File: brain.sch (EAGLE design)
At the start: 9 parts, among them IC1 MCP1253-33X50

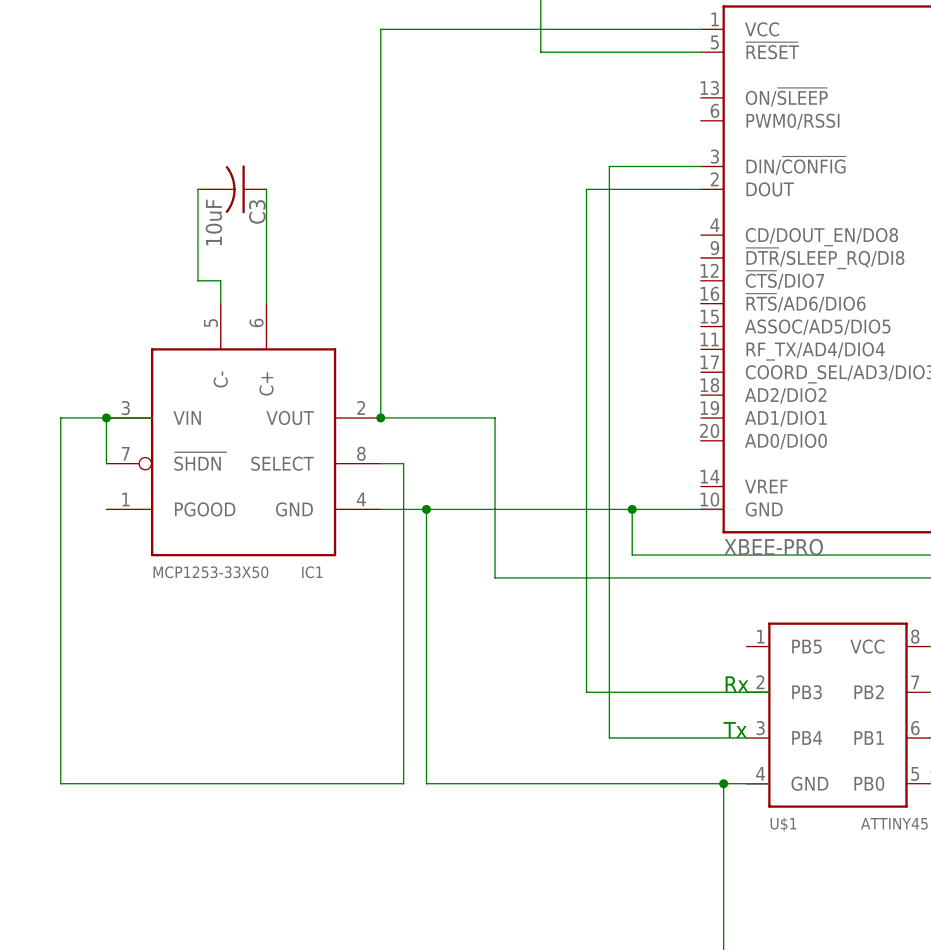
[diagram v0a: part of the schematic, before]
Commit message: Changed to using the TI LDO for the voltage regulation. Created and added symbol for the Sunny Buddy mounting to allow routing tools to see the electrical connections.
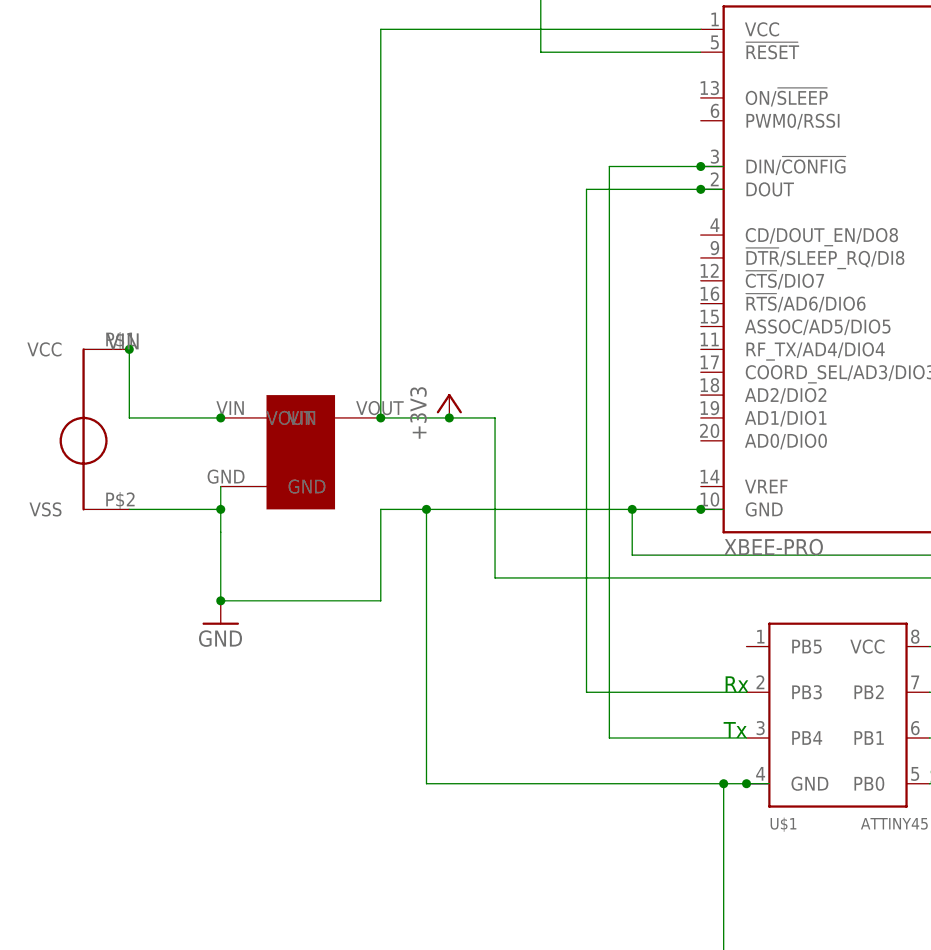
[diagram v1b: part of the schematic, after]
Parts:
- removed C3: 10uF, rcl:C-US050-045X075
- removed IC1: MCP1253-33X50, microchip-MCP125x-xxx:MCP1253-33X50
- added U$2: LP2950, seniordesign:LP2950
- added U$3: SUNNYBUDDYMOUNT, seniordesign:SUNNYBUDDYMOUNT
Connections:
- removed net BAT: IC1.SELECT, IC1.SHDN, IC1.VIN
- removed net N$1: IC1.VOUT, U$1.VCC, XB1.VCC
- removed net N$10: C3.1, IC1.C+
- removed net N$12: C3.2, IC1.C-
- removed net N$5: IC1.GND, R1.2, R2.2, S1.S1
- new net +3V3: U$1.VCC, U$2.VOUT, XB1.VCC
- new net GND: R1.2, R2.2, S1.S1, U$1.GND, U$2.GND, U$3.VSS, XB1.GND
- new net VIN: U$2.VIN, U$3.VCC
- net N$14: now also U$1.PB3
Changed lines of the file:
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@@
 <attribute name="OC_NEWARK" value="unknown"/>
-</part>
-<part name="IC1" library="microchip-MCP125x-xxx" deviceset="MCP1253-33X50" device="">
-<attribute name="MF" value=""/>
-<attribute name="MPN" value="LT3652EMSE#TRPBF"/>
-<attribute name="OC_NEWARK" value="64R8540"/>
 </part>
 <part name="U$1" library="attiny45" deviceset="ATTINY45" device="">
@@
 </part>
 <part name="S1" library="switch-omron" deviceset="10-XX" device=""/>
-<part name="C3" library="rcl" deviceset="C-US" device="050-045X075" value="10uF"/>
 <part name="U2" library="SparkFun-Connectors" deviceset="AUDIO-JACK" device="PTH"/>
 <part name="U3" library="SparkFun-Connectors" deviceset="AUDIO-JACK" device="PTH"/>
+<part name="GND1" library="supply1" deviceset="GND" device=""/>
+<part name="U$2" library="seniordesign" deviceset="LP2950" device=""/>
+<part name="+3V1" library="supply1" deviceset="+3V3" device=""/>
+<part name="U$3" library="seniordesign" deviceset="SUNNYBUDDYMOUNT" device=""/>
 </parts>
 <sheets>
@@
 <instances>
 <instance part="XB1" gate="G$1" x="76.2" y="43.18"/>
-<instance part="IC1" gate="G$1" x="10.16" y="22.86">
-<attribute name="OC_NEWARK" x="10.16" y="22.86" size="1.778" layer="96" display="off"/>
-<attribute name="MF" x="10.16" y="22.86" size="1.778" layer="96" display="off"/>
-<attribute name="MPN" x="10.16" y="22.86" size="1.778" layer="96" display="off"/>
-</instance>
 <instance part="U$1" gate="G$1" x="76.2" y="-7.62">
 <attribute name="OC_NEWARK" x="76.2" y="-7.62" size="1.778" layer="96" display="off"/>
@@
 </instance>
 <instance part="S1" gate="1" x="137.16" y="45.72" rot="R270"/>
-<instance part="C3" gate="G$1" x="10.16" y="50.8" rot="R270"/>
 <instance part="U2" gate="G$1" x="129.54" y="-10.16"/>
 <instance part="U3" gate="G$1" x="129.54" y="-33.02"/>
+<instance part="GND1" gate="1" x="7.62" y="2.54"/>
+<instance part="U$2" gate="G$1" x="17.78" y="20.32"/>
+<instance part="+3V1" gate="G$1" x="33.02" y="27.94"/>
+<instance part="U$3" gate="G$1" x="-7.62" y="25.4"/>
 </instances>
 <busses>
 </busses>
 <nets>
-<net name="N$1" class="0">
-<segment>
-<pinref part="IC1" gate="G$1" pin="VOUT"/>
-<pinref part="XB1" gate="G$1" pin="VCC"/>
-<wire x1="25.4" y1="25.4" x2="25.4" y2="68.58" width="0.1524" layer="91"/>
-<wire x1="25.4" y1="68.58" x2="60.96" y2="68.58" width="0.1524" layer="91"/>
-<pinref part="U$1" gate="G$1" pin="VCC"/>
-<wire x1="86.36" y1="0" x2="88.9" y2="0" width="0.1524" layer="91"/>
-<wire x1="88.9" y1="0" x2="88.9" y2="7.62" width="0.1524" layer="91"/>
-<wire x1="88.9" y1="7.62" x2="38.1" y2="7.62" width="0.1524" layer="91"/>
-<wire x1="38.1" y1="7.62" x2="38.1" y2="25.4" width="0.1524" layer="91"/>
-<wire x1="38.1" y1="25.4" x2="25.4" y2="25.4" width="0.1524" layer="91"/>
-<junction x="25.4" y="25.4"/>
-</segment>
-</net>
 <net name="N$3" class="0">
 <segment>
@@
 </segment>
 </net>
-<net name="N$5" class="0">
-<segment>
-<pinref part="IC1" gate="G$1" pin="GND"/>
+<net name="GND" class="0">
+<segment>
 <wire x1="25.4" y1="15.24" x2="30.48" y2="15.24" width="0.1524" layer="91"/>
-<wire x1="63.5" y1="15.24" x2="53.34" y2="15.24" width="0.1524" layer="91"/>
+<wire x1="63.5" y1="15.24" x2="60.96" y2="15.24" width="0.1524" layer="91"/>
+<wire x1="60.96" y1="15.24" x2="53.34" y2="15.24" width="0.1524" layer="91"/>
 <wire x1="53.34" y1="15.24" x2="30.48" y2="15.24" width="0.1524" layer="91"/>
 <wire x1="30.48" y1="15.24" x2="30.48" y2="-15.24" width="0.1524" layer="91"/>
@@
 <pinref part="R1" gate="G$1" pin="2"/>
 <pinref part="R2" gate="G$1" pin="2"/>
-<wire x1="63.5" y1="-15.24" x2="68.58" y2="-15.24" width="0.1524" layer="91"/>
+<wire x1="63.5" y1="-15.24" x2="66.04" y2="-15.24" width="0.1524" layer="91"/>
+<wire x1="66.04" y1="-15.24" x2="68.58" y2="-15.24" width="0.1524" layer="91"/>
 <wire x1="167.64" y1="-10.16" x2="167.64" y2="-35.56" width="0.1524" layer="91"/>
 <wire x1="167.64" y1="-35.56" x2="167.64" y2="-45.72" width="0.1524" layer="91"/>
@@
 <junction x="167.64" y="-35.56"/>
 <junction x="63.5" y="-15.24"/>
+<wire x1="7.62" y1="17.78" x2="7.62" y2="15.24" width="0.1524" layer="91"/>
+<wire x1="7.62" y1="12.7" x2="7.62" y2="5.08" width="0.1524" layer="91"/>
+<wire x1="7.62" y1="5.08" x2="25.4" y2="5.08" width="0.1524" layer="91"/>
+<wire x1="25.4" y1="5.08" x2="25.4" y2="15.24" width="0.1524" layer="91"/>
+<pinref part="GND1" gate="1" pin="GND"/>
+<junction x="7.62" y="5.08"/>
+<pinref part="U$2" gate="G$1" pin="GND"/>
+<pinref part="XB1" gate="G$1" pin="GND"/>
+<junction x="60.96" y="15.24"/>
+<pinref part="U$1" gate="G$1" pin="GND"/>
+<junction x="66.04" y="-15.24"/>
+<pinref part="U$3" gate="G$1" pin="VSS"/>
+<wire x1="-2.54" y1="15.24" x2="7.62" y2="15.24" width="0.1524" layer="91"/>
+<wire x1="7.62" y1="15.24" x2="7.62" y2="12.7" width="0.1524" layer="91"/>
+<junction x="7.62" y="15.24"/>
 </segment>
 </net>
@@
 <segment>
 <pinref part="XB1" gate="G$1" pin="DIN/!CONFIG"/>
-<wire x1="60.96" y1="53.34" x2="50.8" y2="53.34" width="0.1524" layer="91"/>
+<wire x1="60.96" y1="53.34" x2="58.42" y2="53.34" width="0.1524" layer="91"/>
+<wire x1="58.42" y1="53.34" x2="50.8" y2="53.34" width="0.1524" layer="91"/>
 <wire x1="50.8" y1="53.34" x2="50.8" y2="-10.16" width="0.1524" layer="91"/>
 <pinref part="U$1" gate="G$1" pin="PB4"/>
 <wire x1="50.8" y1="-10.16" x2="66.04" y2="-10.16" width="0.1524" layer="91"/>
+<wire x1="60.96" y1="53.34" x2="63.5" y2="53.34" width="0.1524" layer="91"/>
+<junction x="60.96" y="53.34"/>
 </segment>
 </net>
@@
 <wire x1="60.96" y1="50.8" x2="48.26" y2="50.8" width="0.1524" layer="91"/>
 <wire x1="48.26" y1="50.8" x2="48.26" y2="-5.08" width="0.1524" layer="91"/>
-<wire x1="48.26" y1="-5.08" x2="68.58" y2="-5.08" width="0.1524" layer="91"/>
-</segment>
-</net>
-<net name="BAT" class="0">
-<segment>
-<wire x1="-10.16" y1="-15.24" x2="27.94" y2="-15.24" width="0.1524" layer="91"/>
-<pinref part="IC1" gate="G$1" pin="SHDN"/>
-<wire x1="-5.08" y1="25.4" x2="0" y2="25.4" width="0.1524" layer="91"/>
-<wire x1="-5.08" y1="25.4" x2="-5.08" y2="20.32" width="0.1524" layer="91"/>
-<pinref part="IC1" gate="G$1" pin="VIN"/>
-<junction x="-5.08" y="25.4"/>
-<wire x1="-10.16" y1="25.4" x2="-5.08" y2="25.4" width="0.1524" layer="91"/>
-<wire x1="-10.16" y1="25.4" x2="-10.16" y2="-15.24" width="0.1524" layer="91"/>
-<pinref part="IC1" gate="G$1" pin="SELECT"/>
-<wire x1="25.4" y1="20.32" x2="27.94" y2="20.32" width="0.1524" layer="91"/>
-<wire x1="27.94" y1="20.32" x2="27.94" y2="-15.24" width="0.1524" layer="91"/>
-</segment>
-</net>
-<net name="N$10" class="0">
-<segment>
-<pinref part="IC1" gate="G$1" pin="C+"/>
-<wire x1="12.7" y1="38.1" x2="12.7" y2="50.8" width="0.1524" layer="91"/>
-<pinref part="C3" gate="G$1" pin="1"/>
-</segment>
-</net>
-<net name="N$12" class="0">
-<segment>
-<wire x1="5.08" y1="50.8" x2="5.08" y2="40.64" width="0.1524" layer="91"/>
-<pinref part="IC1" gate="G$1" pin="C-"/>
-<wire x1="5.08" y1="40.64" x2="7.62" y2="40.64" width="0.1524" layer="91"/>
-<wire x1="7.62" y1="40.64" x2="7.62" y2="38.1" width="0.1524" layer="91"/>
-<pinref part="C3" gate="G$1" pin="2"/>
-</segment>
-</net>
+<wire x1="63.5" y1="50.8" x2="60.96" y2="50.8" width="0.1524" layer="91"/>
+<pinref part="U$1" gate="G$1" pin="PB3"/>
+<wire x1="66.04" y1="-5.08" x2="48.26" y2="-5.08" width="0.1524" layer="91"/>
+<junction x="60.96" y="50.8"/>
+</segment>
+</net>
+<net name="VIN" class="0">
+<segment>
+<wire x1="7.62" y1="25.4" x2="-2.54" y2="25.4" width="0.1524" layer="91"/>
+<wire x1="-2.54" y1="25.4" x2="-2.54" y2="33.02" width="0.1524" layer="91"/>
+<label x="-5.08" y="33.02" size="1.778" layer="95"/>
+<pinref part="U$2" gate="G$1" pin="VIN"/>
+<pinref part="U$3" gate="G$1" pin="VCC"/>
+<junction x="-2.54" y="33.02"/>
+<junction x="7.62" y="25.4"/>
+</segment>
+</net>
+<net name="+3V3" class="0">
+<segment>
+<pinref part="XB1" gate="G$1" pin="VCC"/>
+<wire x1="25.4" y1="25.4" x2="25.4" y2="68.58" width="0.1524" layer="91"/>
+<wire x1="25.4" y1="68.58" x2="60.96" y2="68.58" width="0.1524" layer="91"/>
+<pinref part="U$1" gate="G$1" pin="VCC"/>
+<wire x1="86.36" y1="0" x2="88.9" y2="0" width="0.1524" layer="91"/>
+<wire x1="88.9" y1="0" x2="88.9" y2="7.62" width="0.1524" layer="91"/>
+<wire x1="88.9" y1="7.62" x2="38.1" y2="7.62" width="0.1524" layer="91"/>
+<wire x1="38.1" y1="7.62" x2="38.1" y2="25.4" width="0.1524" layer="91"/>
+<wire x1="38.1" y1="25.4" x2="33.02" y2="25.4" width="0.1524" layer="91"/>
+<pinref part="U$2" gate="G$1" pin="VOUT"/>
+<junction x="25.4" y="25.4"/>
+<pinref part="+3V1" gate="G$1" pin="+3V3"/>
+<wire x1="33.02" y1="25.4" x2="25.4" y2="25.4" width="0.1524" layer="91"/>
+<junction x="33.02" y="25.4"/>
+</segment>
+</net>
